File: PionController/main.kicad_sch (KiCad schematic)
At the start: 1 part, among them U1 STM32H743VITx

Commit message: mcu_power
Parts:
- added C12, C13, C20, C21: 2.2uF, Capacitor_SMD:C_0603_1608Metric, symbol Device:C_Small
- added C14, C15, C16, C17, C18, C19, C22, C23: 100nF, Capacitor_SMD:C_0603_1608Metric, symbol Device:C_Small
- added D2: 1N5819W1, Diode_SMD:D_SOD-123, symbol Diode:1N5819WS
- added FB1: 200R/100MHz 500mA, Inductor_SMD:L_0805_2012Metric, symbol Device:FerriteBead_Small
- added R4: 47, symbol Device:R_Small
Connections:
- net +3.3V: now also U1.100 (VDD), U1.11 (VDD), U1.27 (VDD), U1.50 (VDD), U1.6 (VBAT), U1.75 (VDD), C14.1, C15.1, C16.1, C17.1, C18.1, C19.1, D2.1 (K), FB1.1
- net GND: now also C12.1, C13.1, C14.2, C15.2, C16.2, C17.2, C18.2, C19.2, C20.1, C21.2, C22.2, C23.1
- net VREF: now reaches U1.20 (VREF+)
- net VREF: now also C20.2, C22.1, R4.2
- net VDDA: now reaches U1.21 (VDDA)
- net VDDA: now also C21.1, C23.2, D2.2 (A), FB1.2, R4.1
- net at U1.48 (VCAP): now also C12.2
- net at U1.73 (VCAP): now also C13.2
- net Global: no longer names the net of U1.34 (PB0)
- net Local: no longer names the net of U1.35 (PB1)
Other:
- note added: "or SD103AW SOD-123"
- moved on the sheet: U1

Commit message: Schematic_ready
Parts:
- added C24, C25: 22pF, Capacitor_SMD:C_0603_1608Metric, symbol Device:C_Small
- added C26: 2.2uF, Capacitor_SMD:C_0603_1608Metric, symbol Device:C_Small
- added J7: FTSH-107-01-L-DV-K-A, FTSH:SAMTEC_FTSH-107-01-L-DV-K-A, symbol FTSH-107-01-L-DV-K-A:FTSH-107-01-L-DV-K-A
- added R13, R16, R17, R18, R19: 100, Resistor_SMD:R_0603_1608Metric, symbol Device:R_Small
- added R14, R15, R5, R6: 0, Resistor_SMD:R_0603_1608Metric, symbol Device:R_Small
- added R7: 10K, Resistor_SMD:R_0805_2012Metric, symbol Device:R_Small
- added X1: ASE-16.00MHz, Oscillator:Oscillator_SMD_Abracon_ASE-4Pin_3.2x2.5mm, symbol Oscillator:ASE-xxxMHz
- added Y2: 32.768kHZ, Crystal:Crystal_SMD_3215-2Pin_3.2x1.5mm, symbol Device:Crystal
- R4: footprint (none) -> Resistor_SMD:R_0603_1608Metric
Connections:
- net +3.3V: now also C26.2, J7.03, R7.2, X1.4 (Vdd)
- net GND: now also C24.1, C25.1, C26.1, J7.05, J7.07, R13.2, X1.2 (GND)
- net HSE_IN: now reaches U1.12 (PH0)
- net HSE_IN: now also X1.3 (OUT)
- net NRST: now reaches U1.14 (NRST)
- net NRST: now also R19.2
- net RGB_CH_1: now reaches U1.39 (PE9)
- net RGB_CH_2: now reaches U1.41 (PE11)
- net RGB_CH_3: now reaches U1.43 (PE13)
- net RGB_CH_4: now reaches U1.44 (PE14)
- net UART4_RX: now reaches U1.70 (PA11)
- net UART4_RX: now also R15.2
- net UART4_TX: now reaches U1.71 (PA12)
- net UART4_TX: now also R14.2
- net SWDIO: now reaches U1.72 (PA13)
- net SWDIO: now also R16.2
- net SWCLK: now reaches U1.76 (PA14)
- net SWCLK: now also R17.2
- net LSE_OSC_IN: now reaches U1.8 (PC14)
- net LSE_OSC_IN: now also R5.2
- net SWO: now reaches U1.89 (PB3)
- net SWO: now also R18.2
- net LSE_OSC_OUT: now reaches U1.9 (PC15)
- net LSE_OSC_OUT: now also R6.2
- net CAN_COMM_RX: now reaches U1.91 (PB5)
- net CAN_COMM_TX: now reaches U1.92 (PB6)
- net CAN_CRIT_RX: now reaches U1.95 (PB8)
- net CAN_CRIT_TX: now reaches U1.96 (PB9)
- new net: J7.04, R16.1
- new net: J7.06, R17.1
- new net: J7.08, R18.1
- new net: J7.11, R13.1
- new net: J7.12, R19.1
- new net: J7.13, R15.1
- new net: J7.14, R14.1
- new net: R7.1, X1.1 (EN)
- new net: C25.2, R6.1, Y2.1
- new net: C24.2, R5.1, Y2.2
- no-connect marks 0 -> 71
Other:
- note added: "Oscillators"
- note added: "SWDIO"
- moved on the sheet: C20, C21, C22, C23, D2, FB1, R4

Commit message: f
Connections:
- net +3.3V: now also C18.2; no longer C18.1
- net GND: now also C18.1; no longer C18.2
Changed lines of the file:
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@@
 		(lib_id "Device:C_Small")
 		(at 58.42 43.18 0)
-		(mirror y)
+		(mirror x)
 		(unit 1)
 		(exclude_from_sim no)
@@
 		(dnp no)
 		(property "Reference" "C18"
-			(at 55.88 41.9162 0)
+			(at 60.96 44.4438 0)
 			(effects
 				(font
@@
 		)
 		(property "Value" "100nF"
-			(at 55.88 44.4562 0)
+			(at 60.96 41.9038 0)
 			(effects
 				(font

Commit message: Librery fix, 3d models added and fiducial marks
Library Fix: Added missing components and updated footprints, ensuring all parts are properly referenced.
3D Models Added: Integrated 3D models for visual reference in the PCB layout and to assist with mechanical fitment checks.
Fiducial Marks: Placed fiducial marks on the board for accurate alignment during automated assembly processes.
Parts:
- J7: LCSC (none) -> C5563894; MANUFACTURER Samtec -> (none); Manufacturer (none) -> FTSH-107-01-L-DV-K-A
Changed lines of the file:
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@@
 			)
 		)
-		(property "MANUFACTURER" "Samtec"
+		(property "LCSC" "  C5563894"
 			(at 240.03 140.97 0)
 			(effects
@@
 					(size 1.27 1.27)
 				)
-				(justify bottom)
 				(hide yes)
 			)
 		)
-		(property "LCSC" ""
-			(at 240.03 140.97 0)
-			(effects
-				(font
-					(size 1.27 1.27)
-				)
-				(hide yes)
-			)
-		)
-		(property "Manufacturer" ""
+		(property "Manufacturer" " FTSH-107-01-L-DV-K-A "
 			(at 240.03 140.97 0)
 			(effects
@@
 			)
 		)
+		(property "Manufacturer" ""
+			(at 130.81 33.02 0)
+			(effects
+				(font
+					(size 1.27 1.27)
+				)
+				(hide yes)
+			)
+		)
 		(pin "1"
 		)
@@
 			)
 		)
+		(property "Manufacturer" ""
+			(at 130.81 24.13 0)
+			(effects
+				(font
+					(size 1.27 1.27)
+				)
+				(hide yes)
+			)
+		)
 		(pin "1"
 		)
@@
 			(at 97.79 107.95 0)
 			(effects
+				(font
+					(size 1.27 1.27)
+				)
+				(hide yes)
+			)
+		)
+		(property "Comment" ""
+			(at 97.79 107.95 0)
+			(effects

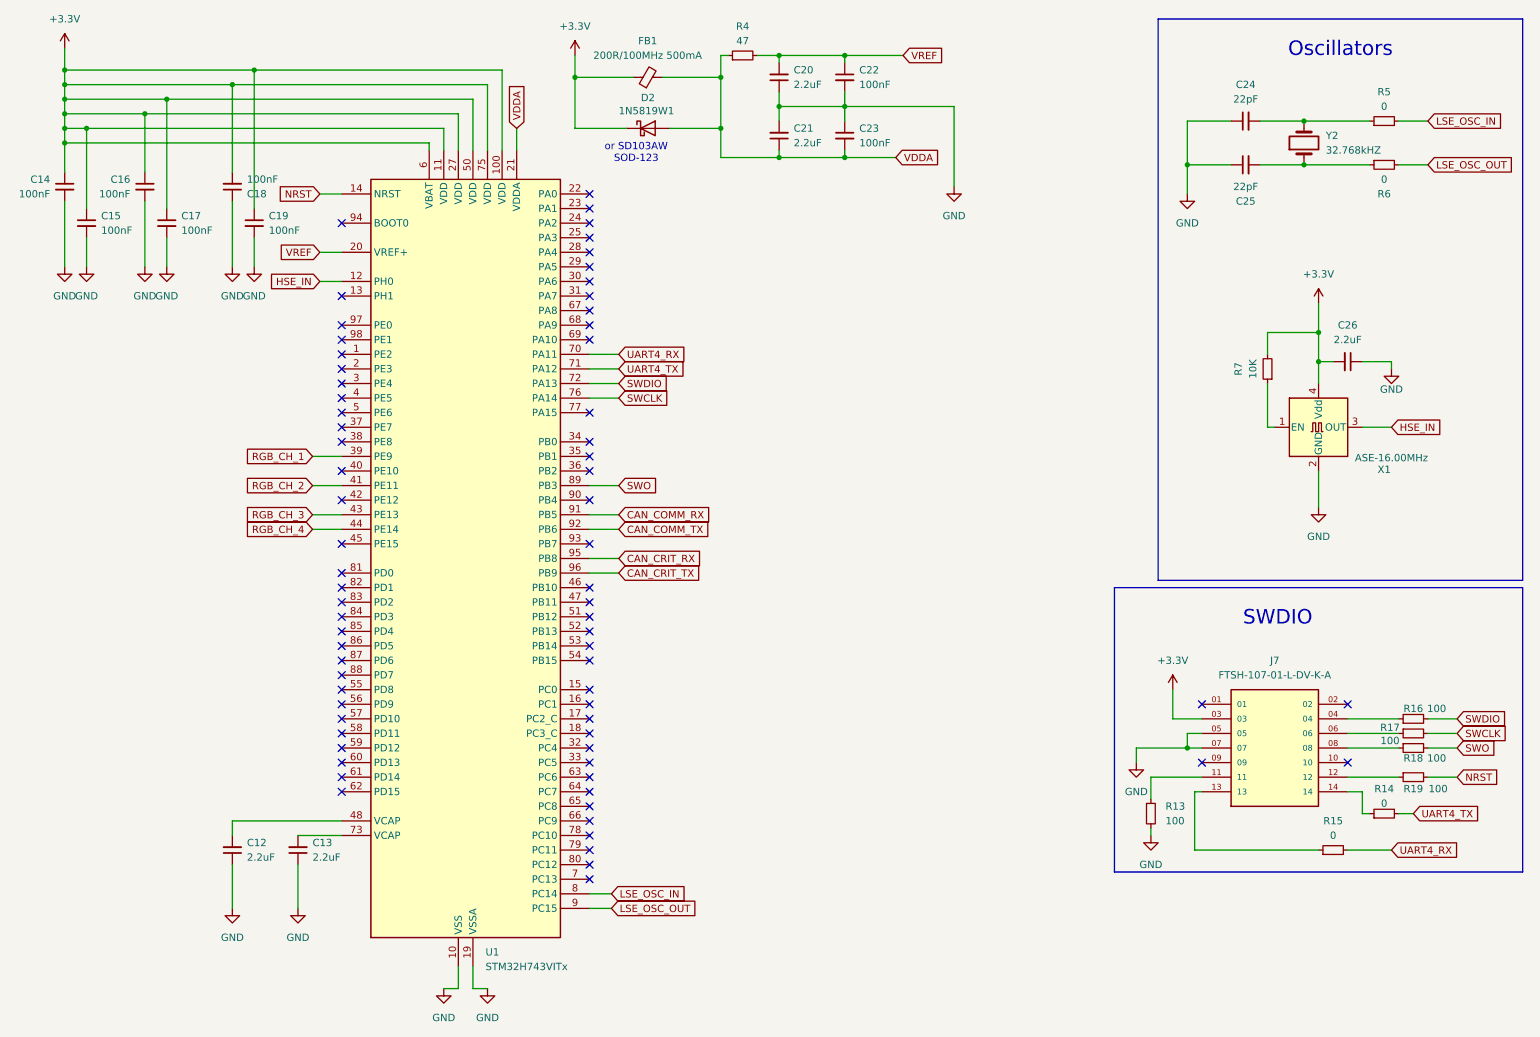
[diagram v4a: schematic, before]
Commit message: Fixing Ivan's remarks and adding the forgotten pull-down resistor
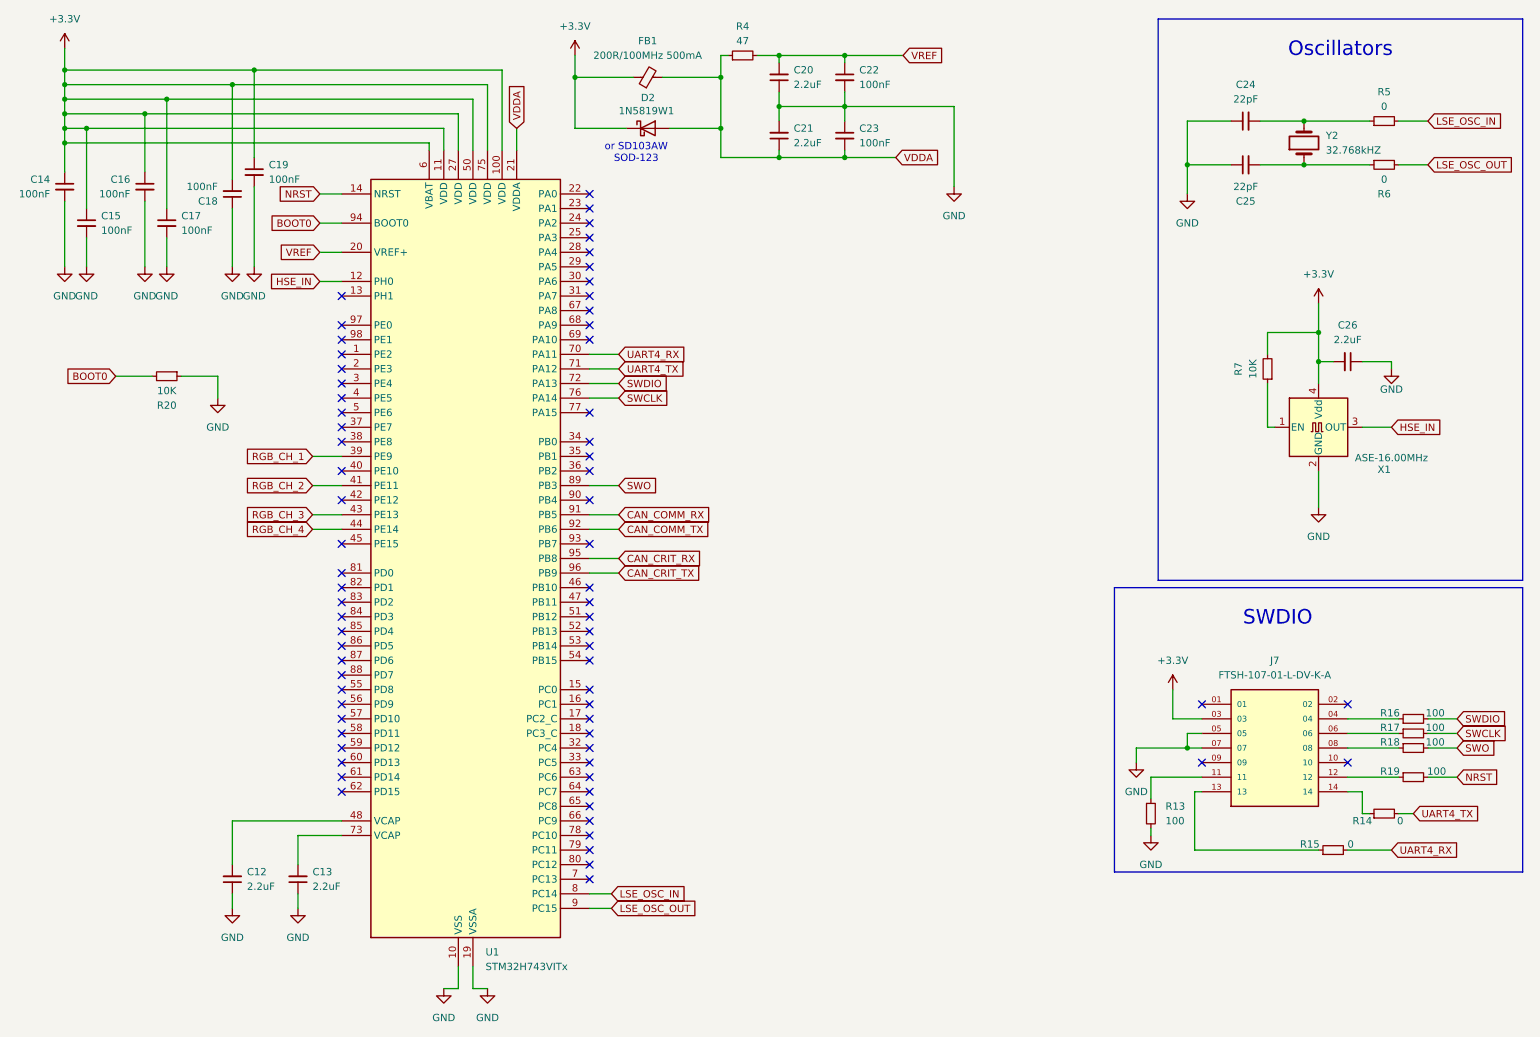
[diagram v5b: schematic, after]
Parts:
- added R20: 10K, Resistor_SMD:R_0805_2012Metric, symbol Device:R_Small
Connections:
- net GND: now also R20.1
- net BOOT0: now reaches U1.94 (BOOT0)
- net BOOT0: now also R20.2
- no-connect marks 71 -> 70
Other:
- moved on the sheet: C12, C13, C18, C19

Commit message: Fixed reference designators in SCH and moved PCB silkscreen positions for better visibility
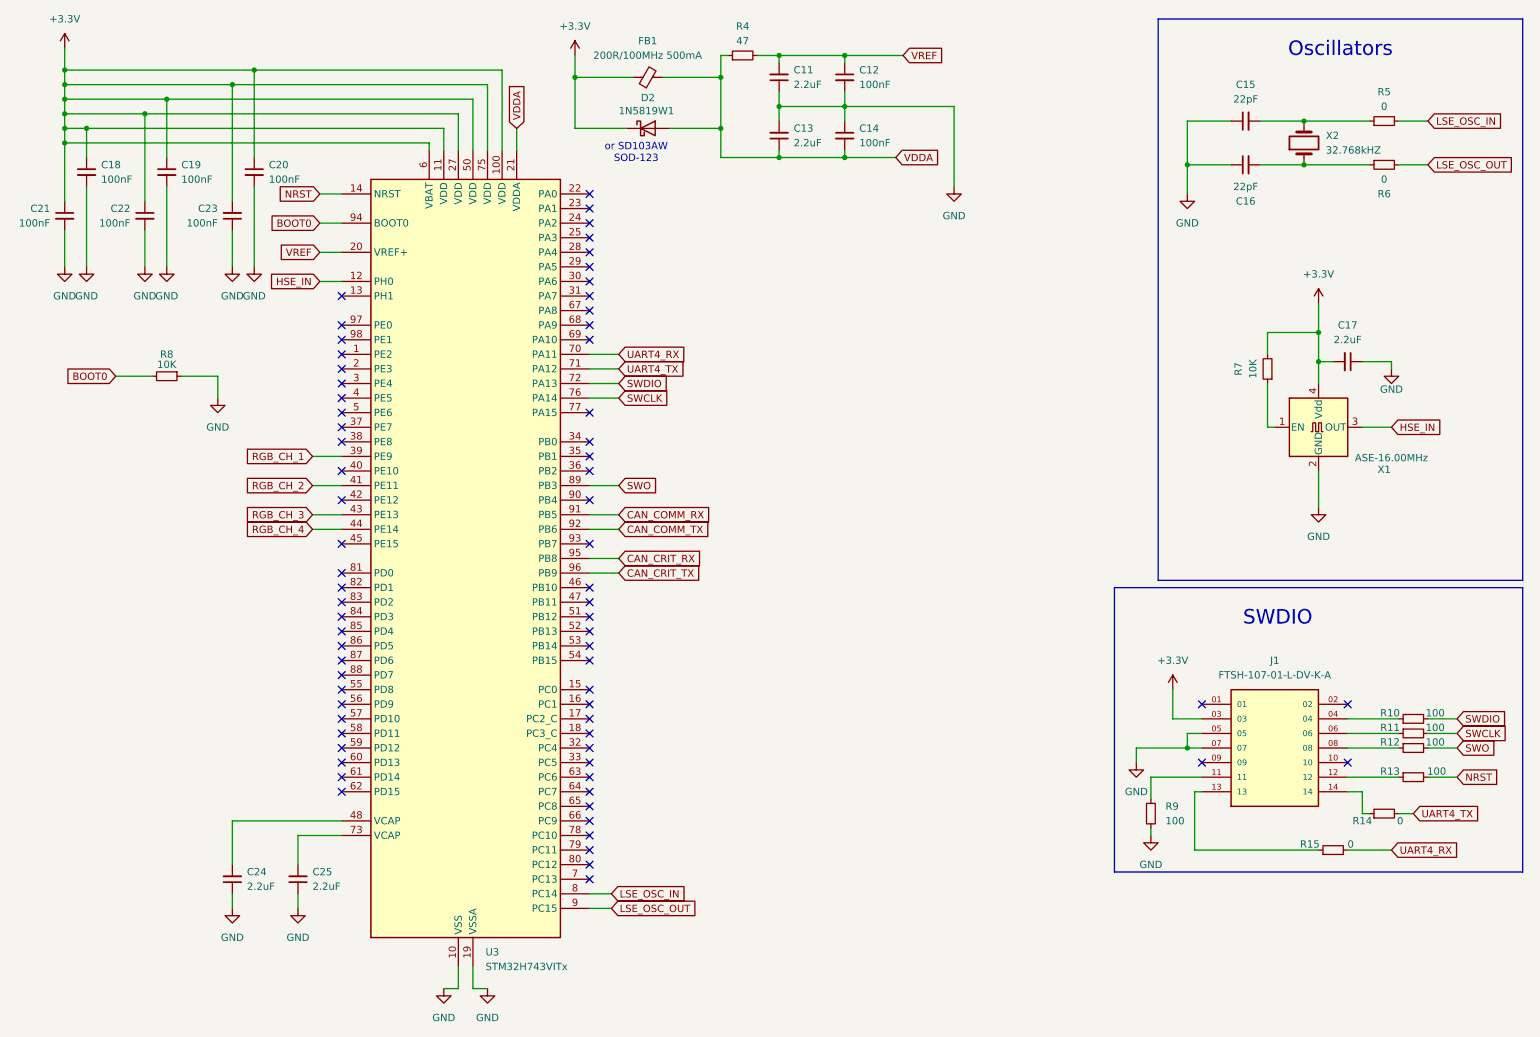
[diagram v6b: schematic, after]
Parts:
- FB1: Manufacturer (none) -> YI201209U201-4R0T
- R7: Manufacturer RC0805FR-0710KL -> RC0805FR-0710KL
- R8: renamed from R20; Manufacturer RC0805FR-0710KL -> RC0805FR-0710KL
- renumbered C20 to C11, C22 to C12, C21 to C13, C23 to C14, C24 to C15, C25 to C16, C26 to C17, C15 to C18, C17 to C19, C19 to C20, C14 to C21, C16 to C22, C18 to C23, C12 to C24, C13 to C25, J7 to J1, R16 to R10, R17 to R11, R18 to R12, R19 to R13, R13 to R9, U1 to U3, Y2 to X2
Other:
- moved on the sheet: C18, C19, C21, C22, C23

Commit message: Added the fabrication files and updated the readme
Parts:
- D2: Manufacturer (none) -> 1N5819W
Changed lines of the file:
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@@
 			)
 		)
-		(property "Manufacturer" ""
+		(property "Manufacturer" "1N5819W"
 			(at 130.81 33.02 0)
 			(effects

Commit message: New version 1.1
Fixing the inductor, the mixed up CPU the resistors, and the  f.silkscreen and b.silkscreen.
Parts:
- U3: LCSC C1235410 -> C114409; Manufacturer stm32f413vgt3 -> STM32H743VIT6
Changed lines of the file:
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@@
 			)
 		)
-		(property "LCSC" "C1235410"
+		(property "LCSC" "C114409"
 			(at 97.79 107.95 0)
 			(effects
@@
 			)
 		)
-		(property "Manufacturer" "stm32f413vgt3"
+		(property "Manufacturer" "STM32H743VIT6"
 			(at 97.79 107.95 0)
 			(effects
